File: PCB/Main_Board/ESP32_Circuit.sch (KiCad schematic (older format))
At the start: 24 parts, among them Q1 MBT3904DW1, SW2 EN, SW3 BOOT, U3 ESP32-WROOM-32, U4 FT231XS

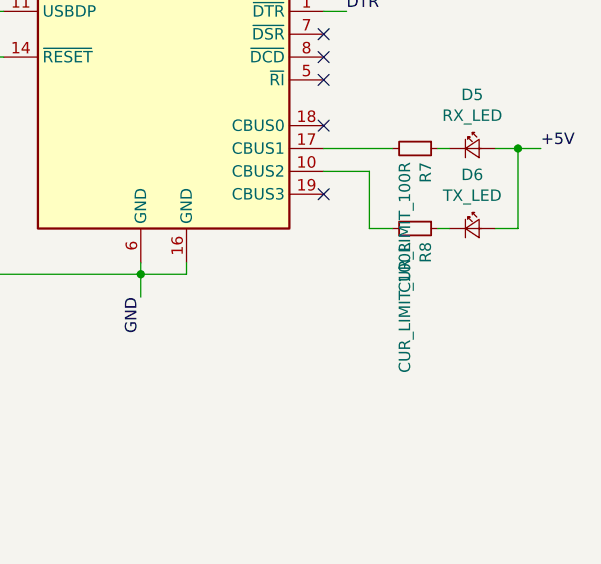
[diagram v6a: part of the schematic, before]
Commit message: Move indicator LED to 5V and increase indicator LED resistors
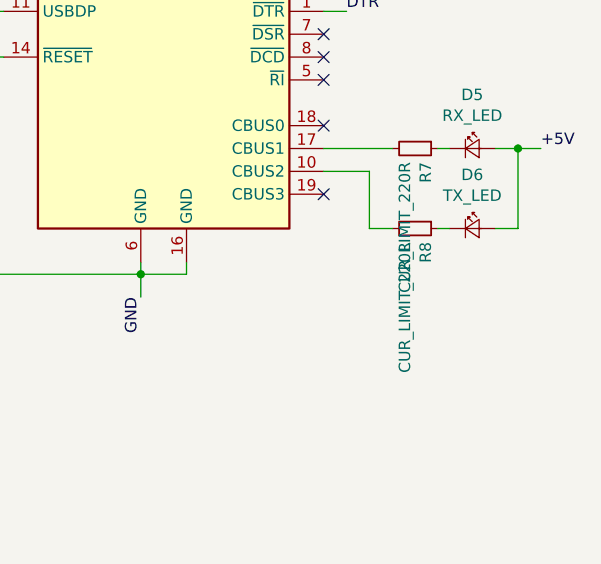
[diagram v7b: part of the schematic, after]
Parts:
- R7, R8: value CUR_LIMIT_100R -> CUR_LIMIT_220R
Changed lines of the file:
@@
 $Descr A4 11693 8268
 encoding utf-8
-Sheet 2 4
+Sheet 4 4
 Title "ESP32 Programming Circuit"
 Date "2020-09-10"
@@
 AR Path="/5F889015/5F5D60DB" Ref="R8"  Part="1"
 F 0 "R8" H 9459 4446 50  0000 L CNN
-F 1 "CUR_LIMIT_100R" H 9459 4355 50  0000 L CNN
+F 1 "CUR_LIMIT_220R" H 9459 4355 50  0000 L CNN
 F 2 "Resistor_SMD:R_0603_1608Metric_Pad1.05x0.95mm_HandSolder" H 9400 4400 50  0001 C CNN
 F 3 "~" H 9400 4400 50  0001 C CNN
@@
 AR Path="/5F889015/5F5D60E8" Ref="R7"  Part="1"
 F 0 "R7" H 9459 4096 50  0000 L CNN
-F 1 "CUR_LIMIT_100R" H 9459 4005 50  0000 L CNN
+F 1 "CUR_LIMIT_220R" H 9459 4005 50  0000 L CNN
 F 2 "Resistor_SMD:R_0603_1608Metric_Pad1.05x0.95mm_HandSolder" H 9400 4050 50  0001 C CNN
 F 3 "~" H 9400 4050 50  0001 C CNN

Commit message: Improve circuit
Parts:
- added R? (x2): 1k, symbol Device:R_Small
- C3: value 0.1uF -> 10uF
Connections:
- net IO1_TXD0: now also R?.2; no longer U4.4 (RXD)
- net IO3_RXD0: now also R?.2; no longer U4.20 (TXD)
- new net: R?.1, U4.20 (TXD)
- new net: R?.1, U4.4 (RXD)
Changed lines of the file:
@@
 	6850 3900 6850 4600
 NoConn ~ 7600 3050
-Text Label 9100 3150 0    50   ~ 0
+Text Label 9600 3150 0    50   ~ 0
 TXD0
-Text Label 9100 3050 0    50   ~ 0
+Text Label 9600 3050 0    50   ~ 0
 RXD0
 Text Label 9100 3250 0    50   ~ 0
@@
 	9000 3250 9100 3250
 Wire Wire Line
-	9000 3150 9100 3150
-Wire Wire Line
 	9000 3050 9100 3050
 Wire Wire Line
@@
 AR Path="/5F889015/5F5F2548" Ref="C3"  Part="1"
 F 0 "C3" H 2042 3146 50  0000 L CNN
-F 1 "0.1uF" H 2042 3055 50  0000 L CNN
+F 1 "10uF" H 2042 3055 50  0000 L CNN
 F 2 "Capacitor_SMD:C_0603_1608Metric_Pad1.05x0.95mm_HandSolder" H 1950 3100 50  0001 C CNN
 F 3 "~" H 1950 3100 50  0001 C CNN
@@
 Connection ~ 7500 3650
 Connection ~ 8400 2700
+$Comp
+L Device:R_Small R?
+U 1 1 5F79186D
+P 9200 3050
+F 0 "R?" V 9396 3050 50  0000 C CNN
+F 1 "1k" V 9305 3050 50  0000 C CNN
+F 2 "" H 9200 3050 50  0001 C CNN
+F 3 "~" H 9200 3050 50  0001 C CNN
+	1    9200 3050
+	0    -1   -1   0
+$EndComp
+$Comp
+L Device:R_Small R?
+U 1 1 5F7A23BF
+P 9400 3150
+F 0 "R?" V 9596 3150 50  0000 C CNN
+F 1 "1k" V 9505 3150 50  0000 C CNN
+F 2 "" H 9400 3150 50  0001 C CNN
+F 3 "~" H 9400 3150 50  0001 C CNN
+	1    9400 3150
+	0    -1   -1   0
+$EndComp
+Wire Wire Line
+	9300 3050 9600 3050
+Wire Wire Line
+	9600 3150 9500 3150
+Wire Wire Line
+	9000 3150 9300 3150
 $EndSCHEMATC
